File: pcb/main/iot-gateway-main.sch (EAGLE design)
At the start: 239 parts, among them CON1 6P-SH-TOP, CON2 2P-PH-TOP, CON3 2P-PH-TOP, CON4 5P-SH-TOP, CON5 3P-SH-TOP, CON6 6P-SH-TOP, Q1 AO3400, Q2 AO3400, Q3 AO3400, T1 BC817, U1 SST26VF064B, U10 BMP280, U11 CCS811, U12 ER-TFT035-6-BOT, U13 74LVC1G17, U14 LT8636, U15 MIC23159, U16 74LVC1G04, U17 LTC4040, U18 FS312F-G, U19 LTC2942, U2 EFM32GG11B820F2048GQ100, U20 FS8205, U21 LTC4313-1, U3 SST26VF016B, U4 ESP8266EX, U5 RFM69HW, U6 74LVC1G08, U7 SIM800C, U8 SI7021, U9 SI7210, X1 8 MHz, X2 32.768 kHz, X3 26 MHz

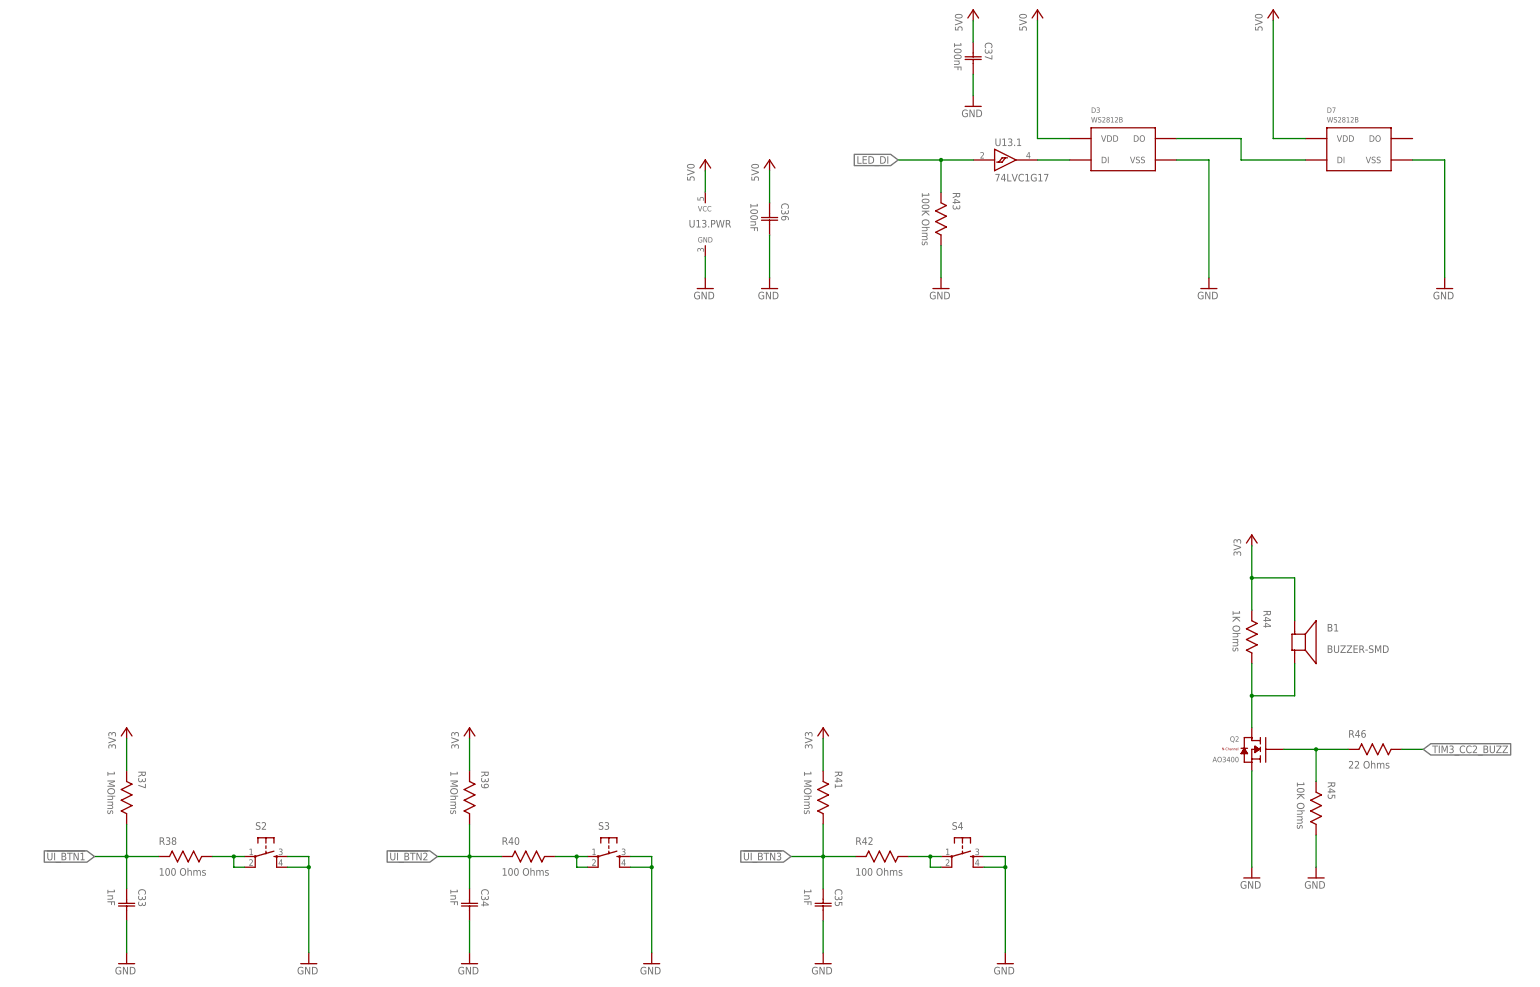
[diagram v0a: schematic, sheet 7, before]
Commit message: Place everything important inside the board space and start routing
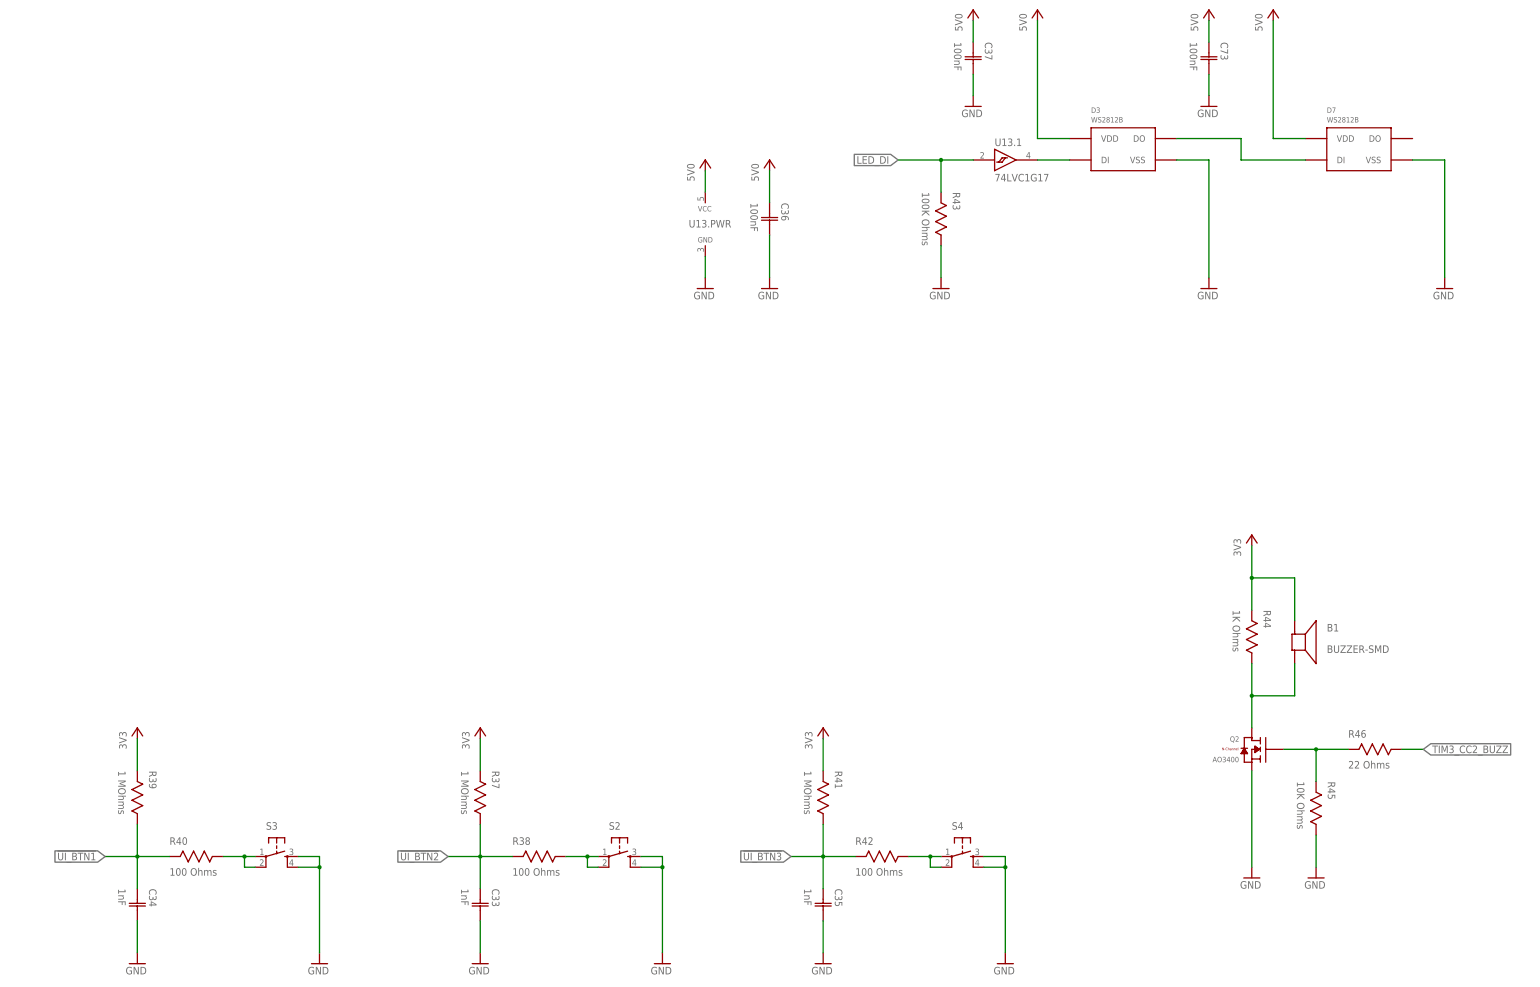
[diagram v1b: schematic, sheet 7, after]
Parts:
- added C72: 10uF, Capacitor:CAPACITOR-0603
- added C73: 100nF, Capacitor:CAPACITOR-0603
- added C74: 22uF, Capacitor:CAPACITOR-1206
- added D8: SP0502BAJT, TVS:SP0502BAJT
- C29: value 100uF -> 10uF; device Capacitor:CAPACITOR-1206 -> Capacitor:CAPACITOR-0603
- C40: VOLTAGE (none) -> 35V
- C42, C43: VOLTAGE (none) -> 50V
- C56: value 10uF -> 100nF
- C63: value 100uF -> 10uF; device Capacitor:ALUMINIUM-CAPACITOR-CASE-D -> Capacitor:CAPACITOR-1206; OCLCSC C97813 -> (none); VOLTAGE 25V -> 50V
- LOGO2: value JS-5MM -> JS-10MM; device Silkscreen:JS-5MM -> Silkscreen:JS-10MM
- X1: value 8 MHz -> 24 MHz
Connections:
- net N$1 renamed CCS811_HEATER_PWM
- net N$10 renamed WIFI_ANT_EXT
- net N$11 renamed WIFI_IO16
- net N$12 renamed 5V0_NBU_NSENS_RT
- net N$13 renamed 5V0_NBU_NSENS_SS
- net N$14 renamed 5V0_NBU_NSENS_INTVCC
- net N$15 renamed 5V0_NBU_NSENS_SW
- net N$17 renamed GSM_LED
- net N$18 renamed SIM_CLK_FILT
- net N$19 renamed LED_DI_BUF
- net N$2 renamed GSM_ANT
- net N$20 renamed BT_ANT
- net N$21 renamed BT_ANT_INT
- net N$22 renamed BT_ANT_EXT
- net N$23 renamed GSM_VRTC
- net N$25 renamed GSM_USB_D-
- net N$26 renamed GSM_USB_D+
- net N$27 renamed !GSM_PWRKEY
- net N$3 renamed SIM_RST_FILT
- net N$30 renamed GSM_USB_VBUS
- net N$31 renamed GSM_2V8
- net N$32 renamed GSM_SPK-
- net N$33 renamed TFT_BACKLIGHT_DRIVER
- net N$35 renamed BUZZ_DRV
- net N$36 renamed 5V0_NBU_NSENS_BST
- net N$38 renamed VBAT_SW
- net N$39 renamed SIM_DATA_FILT
- net N$4 renamed GSM_NETLIGHT
- net N$40 renamed BAT_CHRG_PROG
- net N$41 renamed BAT_PROT_VCC
- net N$42 renamed BAT_PROT_CS
- net N$43 renamed BAT_OC
- net N$44 renamed BAT_OD
- net N$46 renamed 3V3_SW
- net N$47 renamed 3V3_SS
- net N$48 renamed 4V2_SS
- net N$49 renamed 4V2_SW
- net N$5 renamed WIFI_BIAS
- net N$50 renamed MAIN_VREG_SW
- net N$51 renamed GSM_UART2_RX
- net N$52 renamed LED_DO
- net N$54 renamed TFT_BACKLIGHT_PWM
- net N$55 renamed GSM_SPK+
- net N$56 renamed GSM_MIC-
- net N$58 renamed GSM_UART2_TX
- net N$6 renamed WIFI_QSPI_CLK_FILT
- net N$60 renamed GSM_MIC+
- net N$61 renamed WIFI_XTAL_IN
- net N$62 renamed WIFI_XTAL_OUT
- net N$7 renamed WIFI_ANT
- net N$8 renamed WIFI_ANT_FILT
- net N$9 renamed MAIN_VDD_CORE
- net N$90 renamed 5V0_BACKUP
- net !UI_BTN1: now also C34.C1, R39.1, R40.2; no longer C33.C1, R37.1, R38.2
- net !UI_BTN2: now also C33.C1, R37.1, R38.2; no longer C34.C1, R39.1, R40.2
- net 3V3: now also C72.C1, C74.C1
- net 5V0: now also C73.C1
- net GBAT: no longer U19.GND
- net GND: now also C63.C2, C72.C2, C73.C2, C74.C2, D8.A, U19.GND; no longer C63.-
- net MAIN_HFXTAL_N: now also U2.PB14, X1.2; no longer X1.1
- net MAIN_HFXTAL_P: now also U2.PB13, X1.1; no longer X1.2
- net MAIN_LFXTAL_N: now also U2.PB8
- net MAIN_LFXTAL_P: now also U2.PB7
- net USB_D+: now also D8.C1, U2.PF11
- net USB_D-: now also D8.C2, U2.PF10
- net VIN: now also C63.C1; no longer C63.+
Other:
- moved on the sheet: C18, C33, C34, C40, C42, C56, C58, C60, C70, CON4-1, CON4-2, CON4-3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

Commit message: Connect IOs to MCU
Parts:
- removed R91: 100K Ohms, Resistor:RESISTOR-0603
- added C75: 100uF, Capacitor:CAPACITOR-1206
- added C76: 22uF, Capacitor:CAPACITOR-1206
- added U22: FS312F-G, Fortune:FS312F-G
- added U23: FS8205, Fortune:FS8205
- C18, C65: value 100nF -> 22uF; device Capacitor:CAPACITOR-0603 -> Capacitor:CAPACITOR-1206
- C20, C46, C67: value 100uF -> 100nF; device Capacitor:CAPACITOR-1206 -> Capacitor:CAPACITOR-0603
- C21: value 100nF -> 100uF; device Capacitor:CAPACITOR-0603 -> Capacitor:CAPACITOR-1206
- C22: value 33pF -> 100nF
- C23: value 1uF -> 33pF
- C24: value 33pF -> 1uF
- C25: value 100nF -> 33pF
- C29, C66, C72: value 10uF -> 100nF
- C30, C64: value 100nF -> 10uF
- C33, C35: value 1nF -> 100nF
- C37: value 100nF -> 1nF
- C39: value 4.7uF -> 1nF
- C40: value 4.7uF -> 100nF; VOLTAGE 35V -> (none)
- C41: value 470pF -> 100nF
- C42: value 1uF -> 22uF; device Capacitor:CAPACITOR-0603 -> Capacitor:CAPACITOR-1206; VOLTAGE 50V -> (none)
- C43: value 1uF -> 10uF; device Capacitor:CAPACITOR-0603 -> Capacitor:CAPACITOR-1206
- C45: value 1uF -> 22uF; device Capacitor:CAPACITOR-0603 -> Capacitor:CAPACITOR-1206
- C47: value 10nF -> 4.7uF; VOLTAGE (none) -> 35V
- C48: value 470pF -> 4.7uF
- C49: value 470pF -> 1uF; VOLTAGE (none) -> 50V
- C51: value 100nF -> 1uF; VOLTAGE (none) -> 50V
- C52: value 10pF -> 100nF
- C53: value 470pF -> 1uF
- C54: value 470pF -> 100uF; device Capacitor:CAPACITOR-0603 -> Capacitor:CAPACITOR-1206
- C55: value 100uF -> 10nF; device Capacitor:CAPACITOR-1206 -> Capacitor:CAPACITOR-0603
- C56, C58, C61, C71: value 100nF -> 470pF
- C57: value 22uF -> 470pF; device Capacitor:CAPACITOR-1206 -> Capacitor:CAPACITOR-0603
- C60: value 4.7uF -> 10pF
- C63: value 10uF -> 100uF; VOLTAGE 50V -> (none)
- C68, C70: value 22uF -> 100nF; device Capacitor:CAPACITOR-1206 -> Capacitor:CAPACITOR-0603
- C69: value 22uF -> 4.7uF; device Capacitor:CAPACITOR-1206 -> Capacitor:CAPACITOR-0603
- C74: value 22uF -> 10uF; device Capacitor:CAPACITOR-1206 -> Capacitor:CAPACITOR-0603
- CON3: value 2P-PH-TOP -> 6P-SH-TOP; device JST:2P-PH-TOP -> JST:6P-SH-TOP
- CON4: value 5P-SH-TOP -> 3P-SH-TOP; device JST:5P-SH-TOP -> JST:3P-SH-TOP
- CON5: value 3P-SH-TOP -> 5P-SH-TOP; device JST:3P-SH-TOP -> JST:5P-SH-TOP
- CON6: value 6P-SH-TOP -> 2P-PH-TOP; device JST:6P-SH-TOP -> JST:2P-PH-TOP
- D4: value LED1206-REV -> WS2812B; device LED:LED1206-REV -> LED:WS2812B-SMD5050; COLOR GREEN -> (none); PURPOSE Power Indicator -> (none)
- D5: value RED -> SMAJ24A; device LED:LED1206-REV -> TVS:SMAJ24A; COLOR RED -> (none); PURPOSE Backup Indicator -> (none)
- D6: value SMAJ24A -> SP0502BAJT; device TVS:SMAJ24A -> TVS:SP0502BAJT
- D7: value WS2812B -> LED1206-REV; device LED:WS2812B-SMD5050 -> LED:LED1206-REV; COLOR (none) -> GREEN; PURPOSE (none) -> Power Indicator
- D8: value SP0502BAJT -> RED; device TVS:SP0502BAJT -> LED:LED1206-REV; COLOR (none) -> RED; PURPOSE (none) -> Backup Indicator
- R47: value 147K Ohms -> 100K Ohms
- R48: value 21K Ohms -> 100K Ohms
- R50, R51: value 100K Ohms -> 33 Ohms
- R52: value 357K Ohms -> 100K Ohms
- R53: value 61.9K Ohms -> 4.7K Ohms
- R54: value 17.8K Ohms -> 4.7K Ohms
- R56: value 100K Ohms -> 147K Ohms
- R57: value 100K Ohms -> 21K Ohms
- R61: value 100K Ohms -> 357K Ohms
- R62: value 1M Ohms -> 61.9K Ohms
- R63: value 232K Ohms -> 17.8K Ohms
- R64: value 309K Ohms -> 100K Ohms
- R65: value 71.5K Ohms -> 100K Ohms
- R66: value 510 Ohms -> 100K Ohms
- R67: value 178K Ohms -> 100K Ohms
- R68: value 60.4K Ohms -> 100K Ohms
- R70: value 330 Ohms -> 1M Ohms
- R71: value 100K Ohms -> 232K Ohms
- R72: value 100K Ohms -> 309K Ohms
- R73: value 100K Ohms -> 71.5K Ohms
- R74: value 2K Ohms -> 510 Ohms
- R75: value 100K Ohms -> 178K Ohms
- R76: value 10m Ohms -> 60.4K Ohms; device Resistor:RESISTOR-1206 -> Resistor:RESISTOR-0603; OCLCSC C175759 -> (none)
- R77: value 100 Ohms -> 330 Ohms
- R78: value 100 Ohms -> 100K Ohms
- R80: value 1.5M Ohms -> 100K Ohms
- R81: value 274K Ohms -> 100K Ohms
- R82: value 25m Ohms -> 100K Ohms; device Resistor:RESISTOR-1206 -> Resistor:RESISTOR-0603; OCLCSC C127700 -> (none)
- R83: value 100K Ohms -> 2K Ohms
- R84: value 4.7K Ohms -> 100K Ohms
- R85: value 4.7K Ohms -> 25m Ohms; device Resistor:RESISTOR-0603 -> Resistor:RESISTOR-1206; OCLCSC (none) -> C127700
- R86: value 100K Ohms -> 10m Ohms; device Resistor:RESISTOR-0603 -> Resistor:RESISTOR-1206; OCLCSC (none) -> C175759
- R87, R88: value 100K Ohms -> 100 Ohms
- R89: value 33 Ohms -> 1.5M Ohms
- R90: value 33 Ohms -> 274K Ohms
- U13: value 74LVC1G17 -> 74LVC1G08; device Logic:74LVC1G17 -> Logic:74LVC1G08
- U14: value LT8636 -> 74LVC1G08; device Analog Devices:LT8636 -> Logic:74LVC1G08
- U15: value MIC23159 -> 74LVC1G17; device Microchip:MIC23159 -> Logic:74LVC1G17
- U16: value 74LVC1G04 -> LTC4313-1; device Logic:74LVC1G04 -> Analog Devices:LTC4313-1
- U17: value LTC4040 -> LT8636; device Analog Devices:LTC4040 -> Analog Devices:LT8636
- U18: value FS312F-G -> MIC23159; device Fortune:FS312F-G -> Microchip:MIC23159
- U19: value LTC2942 -> 74LVC1G04; device Analog Devices:LTC2942 -> Logic:74LVC1G04
- U20: value FS8205 -> LTC2942; device Fortune:FS8205 -> Analog Devices:LTC2942
- U21: value LTC4313-1 -> LTC4040; device Analog Devices:LTC4313-1 -> Analog Devices:LTC4040
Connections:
- removed net 3V3_PGOOD: R59.1, U15.PG@1
- removed net I2C0_SCL_SENS: R2.1, U10.SCK, U11.SCL, U8.SCL, U9.SCL
- removed net I2C0_SDA_SENS: R1.1, U10.SDI, U11.SDA, U8.SDA, U9.SDA
- removed net I2C1_SCL_SYS: R5.1, U12.X+/SCL, U19.SCL, U21.SCLIN
- removed net I2C1_SDA_SYS: R3.1, U12.Y+/SDA, U19.SDA, U21.SDAIN
- removed net LED_DI: R43.2, U13.1.A
- removed net US0_CS_WIFI: R15.2, U4.MTDO/IO15
- removed net US3_CS_RFM: R18.1, U5.!CS
- removed net WTIM2_CC1_TFT_BL: R30.1
- new net !UI_BTN_IRQ: U14.1.Y, U2.PB1
- new net !US0_CS_WIFI: R15.2, U2.PC8, U4.MTDO/IO15
- new net !US3_CS_RFM: R18.1, U2.PA3, U5.!CS
- new net I2C0_SCL_SYS: R5.1, U12.X+/SCL, U16.SCLIN, U2.PE5, U20.SCL
- new net I2C0_SDA_SYS: R3.1, U12.Y+/SDA, U16.SDAIN, U2.PE4, U20.SDA
- new net I2C1_SCL_SENS: R2.1, U10.SCK, U11.SCL, U2.PC5, U8.SCL, U9.SCL
- new net I2C1_SDA_SENS: R1.1, U10.SDI, U11.SDA, U2.PC4, U8.SDA, U9.SDA
- new net N$1: U13.1.Y, U14.1.A
- new net TIM4_CC2_LED_DI: R43.2, U15.1.A, U2.PF12
- new net WTIM2_CC2_TFT_BL: R30.1, U2.PA11
- net !5V0_BACKUP: now also R78.1, U19.1.A, U2.PC7, U21.!PFO; no longer R71.1, U16.1.A, U17.!PFO
- net !BAT_CHRG: now also R82.1, U2.PD7, U21.!CHRG; no longer R75.1, U17.!CHRG
- net !BAT_CHRG_EN: now also R84.1, U2.PD8, U21.CHGOFF; no longer R88.1, U17.CHGOFF
- net !BAT_FAULT: now also R81.1, U2.PD6, U21.!FAULT; no longer R73.1, U17.!FAULT
- net !CCS811_IRQ: now also U2.PE13
- net !CCS811_RESET: now also U2.PE14
- net !CCS811_WAKE: now also U2.PE12
- net !FUEL_GAUGE_IRQ: now also U2.PE10, U20.!AL!/CC; no longer U19.!AL!/CC
- net !GSM_DTR: now also U2.PC2
- net !GSM_RING: now also U2.PC1
- net !TFT_RESET: now also U2.PA14
- net !TFT_TOUCH_IRQ: now also U2.PA12
- net !TFT_TOUCH_RESET: now also U2.PA13
- net !UI_BTN1: now also R37.1, R38.2, U13.1.A, U2.PB2; no longer R39.1, R40.2
- net !UI_BTN2: now also C37.C1, R39.1, R40.2, U13.1.B, U2.PB3; no longer C33.C1, R37.1, R38.2
- net !UI_BTN3: now also C39.C1, U14.1.B, U2.PB4; no longer C35.C1
- net !US2_CS_TFT: now also U2.PA10
- net !USB_PD_IRQ: now also CON3-2.S, R49.1, U2.PE1; no longer CON6-2.S, R83.1
- net !USB_VBUS_HV_EN: now also CON5-3.S, U2.PF9; no longer CON4-3.S
- net !WIFI_RESET: now also U2.PF5
- net 3V3: now also C19.C1, C22.C1, C33.C1, C35.C1, C36.C1, C42.C1, C44.C1, C64.C1, C66.C1, C70.C1, CON3-1.S, R48.2, R49.2, R52.2, R53.2, R54.2, R65.2, R78.2, R80.2, R81.2, R82.2, U13.PWR.VCC, U14.PWR.VCC, U16.VCC, U18.SNS@1, U19.PWR.VCC; no longer C21.C1, C25.C1, C56.C1, C61.C1, C69.C1, C71.C1, C72.C1, C74.C1, CON6-1.S, R56.2, R59.2, R69.2, R71.2, R73.2, R75.2, R83.2, R85.2, R86.2, R88.2, R91.2, U15.SNS@1, U16.PWR.VCC, U21.VCC
- net 3V3_FB: now also R72.1, R73.2, U18.FB@1; no longer R64.1, R65.2, U15.FB@1
- net 3V3_SS: now also C61.C1, U18.SS@1; no longer C53.C1, U15.SS@1
- net 3V3_SW: now also U18.SW@1; no longer U15.SW@1
- net 4V2: now also C21.C1, C52.C1, C54.C1, R59.2, R61.2, U18.SNS@0; no longer C19.C1, C44.C1, C46.C1, R50.2, R52.2, U15.SNS@0
- net 4V2_EN: now also R58.2, U18.EN@0, U2.PB0; no longer R49.2, U15.EN@0
- net 4V2_FB: now also R61.1, R62.2, U18.FB@0; no longer R52.1, R53.2, U15.FB@0
- net 4V2_PGOOD: now also R65.1, U18.PG@0, U2.PE11; no longer R56.1, U15.PG@0
- net 4V2_SS: now also C57.C1, U18.SS@0; no longer C49.C1, U15.SS@0
- net 4V2_SW: now also U18.SW@0; no longer U15.SW@0
- net 4V2_VSENSE: now also C56.C1, R59.1, R60.2, U2.PD2; no longer C48.C1, R50.1, R51.2
- net 5V0: now also C40.C1, C41.C1, C45.C1, C46.C1, C48.C1, C69.C1, C75.C1, C76.C1, CON5-1.S, D4.VDD, R66.2, R89.2, U15.PWR.VCC, U18.AVIN@0, U18.AVIN@1, U18.EN@1, U18.VIN@0, U18.VIN@1, U21.F0, U21.F1, U21.F2, U21.VSYS; no longer C36.C1, C37.C1, C39.C1, C58.C1, C60.C1, C67.C1, C70.C1, C73.C1, CON4-1.S, D7.VDD, R57.2, R80.2, U13.PWR.VCC, U15.AVIN@0, U15.AVIN@1, U15.EN@1, U15.VIN@0, U15.VIN@1, U17.F0, U17.F1, U17.F2, U17.VSYS
- net 5V0_BACKUP: now also R77.2, U19.1.Y; no longer R70.2, U16.1.Y
- net 5V0_FB: now also R89.1, R90.2, U21.BSTFB, U21.RSTFB; no longer R80.1, R81.2, U17.BSTFB, U17.RSTFB
- net 5V0_ISENSE: now also C71.C1, U2.PD5, U21.CLPROG; no longer C62.C1, U17.CLPROG
- net 5V0_NBU: now also R86.1, U21.CLN; no longer R76.1, U17.CLN
- net 5V0_NBU_NSENS: now also C60.C1, C63.C1, C65.C1, C67.C1, R70.2, R74.2, R75.2, R86.2, U17.BIAS, U21.OVSNS, U21.VIN; no longer C52.C1, C55.C1, C57.C1, C59.C1, R62.2, R66.2, R67.2, R76.2, U14.BIAS, U17.OVSNS, U17.VIN
- net 5V0_NBU_NSENS_BST: now also C59.C2, U17.BST; no longer C51.C2, U14.BST
- net 5V0_NBU_NSENS_FB: now also C60.C2, R70.1, R71.2, U17.FB; no longer C52.C2, R62.1, R63.2, U14.FB
- net 5V0_NBU_NSENS_INTVCC: now also C53.C1, U17.INTVCC, U17.SYNC/MODE; no longer C45.C1, U14.INTVCC, U14.SYNC/MODE
- net 5V0_NBU_NSENS_PGOOD: now also R64.1, U17.PG, U2.PD0; no longer R55.1, U14.PG
- net 5V0_NBU_NSENS_RT: now also R63.2, U17.RT; no longer R54.2, U14.RT
- net 5V0_NBU_NSENS_SS: now also C55.C1, U17.TR/SS; no longer C47.C1, U14.TR/SS
- net 5V0_NBU_NSENS_SW: now also C59.C1, U17.SW; no longer C51.C1, U14.SW
- net 5V0_PGOOD: now also R80.1, U2.PA6, U21.!RST; no longer R72.1, U17.!RST
- net 5V0_VSENSE: now also C58.C1, R66.1, R67.2, U2.PD3; no longer C50.C1, R57.1, R58.2
- net BAT_CHRG_PROG: now also R83.2, U21.PROG; no longer R74.2, U17.PROG
- net BAT_OC: now also U22.OC, U23.G1; no longer U18.OC, U20.G1
- net BAT_OD: now also U22.OD, U23.G2; no longer U18.OD, U20.G2
- net BAT_PROT_CS: now also R88.2, U22.CS; no longer R78.2, U18.CS
- net BAT_PROT_VCC: now also R87.1, U22.VCC; no longer R77.1, U18.VCC
- net DCJACK_DET: now also CON3-5.S, R48.1, U2.PE8; no longer CON6-5.S, R69.1
- net GBAT: now also C72.C2, CON6-2.S, U22.GND, U23.S2; no longer C64.C2, CON2-2.S, U18.GND, U20.S2
- net GND: now also C51.C2, C52.C2, C64.C2, C75.C2, C76.C2, CON2-2.S, CON3-6.S, CON4-3.S, CON5-5.S, D4.VSS, D5.A, D7.C, D8.C, R47.1, R57.1, R60.1, R62.1, R67.1, R69.1, R71.1, R73.1, R76.1, R83.1, R88.1, R90.1, U14.PWR.GND, U15.PWR.GND, U16.GND, U18.AGND@0, U18.AGND@1, U18.PGND@0, U18.PGND@1, U18.PGND@2, U19.PWR.GND, U20.GND, U21.BSTOFF, U21.NTC, U23.S1; no longer C59.C2, C60.C2, C72.C2, CON3-2.S, CON4-5.S, CON5-3.S, CON6-6.S, D4.C, D5.C, D7.VSS, D8.A, R48.1, R49.1, R51.1, R53.1, R54.1, R61.1, R65.1, R68.1, R74.1, R78.1, R81.1, R87.1, U14.GND, U15.AGND@0, U15.AGND@1, U15.PGND@0, U15.PGND@1, U15.PGND@2, U16.PWR.GND, U17.BSTOFF, U17.NTC, U19.GND, U20.S1
- net GSM_LED_EN: now also U2.PB5
- net GSM_PWRKEY: now also U2.PB6
- net GSM_RF_SYNC: now also U2.PC0
- net GSM_STATUS: now also U2.PC3
- net I2C_SCL_USB_PD: now also CON3-3.S, R54.1, U16.SCLOUT; no longer CON6-3.S, R85.1, U21.SCLOUT
- net I2C_SDA_USB_PD: now also CON3-4.S, R53.1, U16.SDAOUT; no longer CON6-4.S, R84.1, U21.SDAOUT
- net LED_DI_BUF: now also U15.1.Y; no longer U13.1.Y
- net LED_DO: now also D4.DI; no longer D7.DI
- net MAG_ALERT: now also U2.PE15
- net N$37: now also U21.IGATE; no longer U17.IGATE
- net N$63: now also CON4-2.S, R51.2; no longer CON5-2.S, R90.2
- net N$64: now also CON4-1.S, R50.2; no longer CON5-1.S, R89.2
- net N$91: now also D7.A, R74.1; no longer D4.A, R66.1
- net N$92: now also D8.A, R77.1; no longer D5.A, R70.1
- net PF_THRESH: now also R75.1, R76.2, U21.PFI; no longer R67.1, R68.2, U17.PFI
- net RFM_IRQ: now also U2.PA5
- net RFM_RESET: now also U2.PA4
- net SIM_DATA: now also C25.C1; no longer C24.C1
- net SIM_VDD: now also C24.C1; no longer C22.C1
- net TIM3_CC2_BUZZ: now also U2.PA15
- net U0_CTS_GSM: now also U2.PB11
- net U0_RTS_GSM: now also U2.PB12
- net U0_RX_GSM: now also U2.PB10
- net U0_TX_GSM: now also U2.PB9
- net US0_CLK_WIFI: now also U2.PC9
- net US0_MISO_WIFI: now also U2.PC10
- net US0_MOSI_WIFI: now also U2.PC11
- net US2_CLK_TFT: now also U2.PA9
- net US2_MISO_TFT: now also U2.PA8
- net US2_MOSI_TFT: now also U2.PA7
- net US3_CLK_RFM: now also U2.PA2
- net US3_MISO_RFM: now also U2.PA1
- net US3_MOSI_RFM: now also U2.PA0
- net USB_D+: now also D6.C1, R50.1; no longer D8.C1, R89.1
- net USB_D-: now also D6.C2, R51.1; no longer D8.C2, R90.1
- net USB_PD_I2C_EN: now also R47.2, U16.ENABLE, U2.PE2; no longer R87.2, U21.ENABLE
- net USB_PD_I2C_READY: now also R52.1, U16.READY, U2.PE3; no longer R86.1, U21.READY
- net USB_VBUS_HV_STAT: now also CON5-2.S, R55.1, U2.PF8; no longer CON4-2.S, R91.1
- net USB_VBUS_SUP_EN: now also CON5-4.S, U2.PE9; no longer CON4-4.S
- net VBAT: now also C72.C1, C73.C1, C74.C1, R68.2, R85.2, R87.2, U20.VDD/SENSE+, U21.BAT; no longer C64.C1, C65.C1, C66.C1, R60.2, R77.2, R82.2, U17.BAT, U19.VDD/SENSE+
- net VBAT_NSENS: now also CON6-1.S, R85.1, U20.VBAT/SENSE-; no longer CON2-1.S, R82.1, U19.VBAT/SENSE-
- net VBAT_SW: now also U21.SW; no longer U17.SW
- net VBAT_VSENSE: now also C62.C1, R68.1, R69.2, U2.PD4; no longer C54.C1, R60.1, R61.2
- net VIN: now also C47.C1, C49.C1, C51.C1, D5.C, R56.2, U17.EN/UV, U17.VIN; no longer C40.C1, C42.C1, C63.C1, D6.C, R47.2, U14.EN/UV, U14.VIN
- net VIN_UNFUSED: now also CON2-1.S; no longer CON3-1.S
- net VIN_VSENSE: now also C50.C1, R56.1, R57.2, U2.PD1; no longer C41.C1, R47.1, R48.2
- net WIFI_EN: now also U2.PE6
- net WIFI_IRQ: now also U2.PE7

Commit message: Update libraries Finish routing Generate schematic PDF files
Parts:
- removed SJ1: (no value), Solder Jumper:SJS
- added C77: 10uF, Capacitor:CAPACITOR-0603
- added C78: 100uF, Capacitor:CAPACITOR-1206
- added C79: 22uF, Capacitor:CAPACITOR-1206
- added CON7: 2P-PH-TOP, JST:2P-PH-TOP
- added R91: 100K Ohms, Resistor:RESISTOR-0603
- added R92: 25m Ohms, Resistor:RESISTOR-1206
- added R93: 10m Ohms, Resistor:RESISTOR-1206
- added R94, R95: 100 Ohms, Resistor:RESISTOR-0603
- added R96: 1.5M Ohms, Resistor:RESISTOR-0603
- added R97: 274K Ohms, Resistor:RESISTOR-0603
- added U24: LTC4040, Analog Devices:LTC4040
- added U25: FS312F-G, Fortune:FS312F-G
- added U26: FS8205, Fortune:FS8205
- C21, C75: value 100uF -> 100nF; device Capacitor:CAPACITOR-1206 -> Capacitor:CAPACITOR-0603
- C22, C66: value 100nF -> 100uF; device Capacitor:CAPACITOR-0603 -> Capacitor:CAPACITOR-1206
- C23: value 33pF -> 100nF
- C24: value 1uF -> 33pF
- C25: value 33pF -> 1uF
- C26: value 100nF -> 33pF
- C30: value 10uF -> 100nF
- C31: value 100nF -> 1uF
- C33, C67: value 100nF -> 10uF
- C34, C39: value 1nF -> 100nF
- C38, C41: value 100nF -> 1nF
- C42, C76: value 22uF -> 100nF; device Capacitor:CAPACITOR-1206 -> Capacitor:CAPACITOR-0603
- C43: value 10uF -> 100nF; device Capacitor:CAPACITOR-1206 -> Capacitor:CAPACITOR-0603; VOLTAGE 50V -> (none)
- C46: value 100nF -> 10uF; device Capacitor:CAPACITOR-0603 -> Capacitor:CAPACITOR-1206; VOLTAGE (none) -> 50V
- C47: value 4.7uF -> 100nF; VOLTAGE 35V -> (none)
- C48: value 4.7uF -> 22uF; device Capacitor:CAPACITOR-0603 -> Capacitor:CAPACITOR-1206
- C49: value 1uF -> 100nF; VOLTAGE 50V -> (none)
- C50: value 470pF -> 4.7uF; VOLTAGE (none) -> 35V
- C51: value 1uF -> 4.7uF; VOLTAGE 50V -> (none)
- C52: value 100nF -> 1uF; VOLTAGE (none) -> 50V
- C53: value 1uF -> 470pF
- C54: value 100uF -> 1uF; device Capacitor:CAPACITOR-1206 -> Capacitor:CAPACITOR-0603; VOLTAGE (none) -> 50V
- C55: value 10nF -> 100nF
- C56: value 470pF -> 1uF
- C57: value 470pF -> 100uF; device Capacitor:CAPACITOR-0603 -> Capacitor:CAPACITOR-1206
- C58: value 470pF -> 10nF
- C59: value 100nF -> 470pF
- C60: value 10pF -> 470pF
- C62, C71: value 470pF -> 100nF
- C63: value 100uF -> 10pF; device Capacitor:CAPACITOR-1206 -> Capacitor:CAPACITOR-0603
- C64, C74: value 10uF -> 470pF
- C65: value 22uF -> 470pF; device Capacitor:CAPACITOR-1206 -> Capacitor:CAPACITOR-0603
- C68: value 100nF -> 22uF; device Capacitor:CAPACITOR-0603 -> Capacitor:CAPACITOR-1206
- C69: value 4.7uF -> 100nF
- C72: value 100nF -> 4.7uF
- CON2: value 2P-PH-TOP -> 3P-SH-TOP; device JST:2P-PH-TOP -> JST:3P-SH-TOP
- CON3: value 6P-SH-TOP -> 2P-PH-TOP; device JST:6P-SH-TOP -> JST:2P-PH-TOP
- CON4: value 3P-SH-TOP -> 6P-SH-TOP; device JST:3P-SH-TOP -> JST:6P-SH-TOP
- CON5: value 5P-SH-TOP -> 3P-SH-TOP; device JST:5P-SH-TOP -> JST:3P-SH-TOP
- CON6: value 2P-PH-TOP -> 5P-SH-TOP; device JST:2P-PH-TOP -> JST:5P-SH-TOP
- R1, R2, R3, R5: value 4.7K Ohms -> 2.2K Ohms
- R17: value 10K Ohms -> 0 Ohms
- R18, R34, R35: value 100K Ohms -> 10K Ohms
- R20, R77: value 330 Ohms -> 100K Ohms
- R21: value 10K Ohms -> 100K Ohms
- R22, R23: value 0 Ohms -> 100K Ohms
- R24, R25: value 22 Ohms -> 100K Ohms
- R26, R30: value 22 Ohms -> 0 Ohms
- R27: value 10K Ohms -> 330 Ohms
- R29: value 100K Ohms -> 0 Ohms
- R31: value 10K Ohms -> 22 Ohms
- R32: value 0 Ohms -> 22 Ohms
- R33: value 100K Ohms -> 22 Ohms
- R37, R41: value 1 MOhms -> 100K Ohms
- R38: value 100 Ohms -> 22 Ohms
- R39: value 1 MOhms -> 10K Ohms
- R40: value 100 Ohms -> 0 Ohms
- R42, R87, R88: value 100 Ohms -> 100K Ohms
- R44: value 1K Ohms -> 100K Ohms; MF VISHAY -> (none)
- R45: value 10K Ohms -> 1 MOhms; MF VISHAY -> (none)
- R46: value 22 Ohms -> 100 Ohms; MF VISHAY -> (none)
- R47: value 100K Ohms -> 1 MOhms
- R48: value 100K Ohms -> 100 Ohms
- R50: value 33 Ohms -> 1 MOhms
- R51: value 33 Ohms -> 100 Ohms
- R52: value 100K Ohms -> 1K Ohms; MF (none) -> VISHAY
- R53: value 4.7K Ohms -> 10K Ohms; MF (none) -> VISHAY
- R54: value 4.7K Ohms -> 22 Ohms; MF (none) -> VISHAY
- R56: value 147K Ohms -> 100K Ohms
- R57: value 21K Ohms -> 100K Ohms
- R58, R59: value 100K Ohms -> 33 Ohms
- R61: value 357K Ohms -> 4.7K Ohms
- R62: value 61.9K Ohms -> 4.7K Ohms
- R63: value 17.8K Ohms -> 100K Ohms
- R64: value 100K Ohms -> 147K Ohms
- R65: value 100K Ohms -> 21K Ohms
- R69: value 100K Ohms -> 357K Ohms
- R70: value 1M Ohms -> 61.9K Ohms
- R71: value 232K Ohms -> 17.8K Ohms
- R72: value 309K Ohms -> 100K Ohms
- R73: value 71.5K Ohms -> 100K Ohms
- R74: value 510 Ohms -> 100K Ohms
- R75: value 178K Ohms -> 100K Ohms
- R76: value 60.4K Ohms -> 100K Ohms
- R78: value 100K Ohms -> 1M Ohms
- R79: value 100K Ohms -> 232K Ohms
- R80: value 100K Ohms -> 309K Ohms
- R81: value 100K Ohms -> 71.5K Ohms
- R82: value 100K Ohms -> 510 Ohms
- R83: value 2K Ohms -> 178K Ohms
- R84: value 100K Ohms -> 57.6K Ohms
- R85: value 25m Ohms -> 330 Ohms; device Resistor:RESISTOR-1206 -> Resistor:RESISTOR-0603; OCLCSC C127700 -> (none)
- R86: value 10m Ohms -> 100K Ohms; device Resistor:RESISTOR-1206 -> Resistor:RESISTOR-0603; OCLCSC C175759 -> (none)
- R89: value 1.5M Ohms -> 100K Ohms
- R90: value 274K Ohms -> 2K Ohms
- U10: value BMP280 -> SIM800C; device Bosch:BMP280 -> SimCom:SIM800C
- U11: value CCS811 -> SI7021; device AMS:CCS811 -> Silicon Labs:SI7021
- U12: value ER-TFT035-6-BOT -> SI7210; device BuyDisplay:ER-TFT035-6-BOT -> Silicon Labs:SI7210
- U13: value 74LVC1G08 -> BMP280; device Logic:74LVC1G08 -> Bosch:BMP280
- U14: value 74LVC1G08 -> CCS811; device Logic:74LVC1G08 -> AMS:CCS811
- U15: value 74LVC1G17 -> TMG39933; device Logic:74LVC1G17 -> AMS:TMG39933
- U16: value LTC4313-1 -> ER-TFT035-6-BOT; device Analog Devices:LTC4313-1 -> BuyDisplay:ER-TFT035-6-BOT
- U17: value LT8636 -> 74LVC1G11; device Analog Devices:LT8636 -> Logic:74LVC1G11
- U18: value MIC23159 -> 74LVC1G17; device Microchip:MIC23159 -> Logic:74LVC1G17
- U19: value 74LVC1G04 -> LTC4313-1; device Logic:74LVC1G04 -> Analog Devices:LTC4313-1
- U20: value LTC2942 -> LT8636; device Analog Devices:LTC2942 -> Analog Devices:LT8636
- U21: value LTC4040 -> MIC23159; device Analog Devices:LTC4040 -> Microchip:MIC23159
- U22: value FS312F-G -> 74LVC1G04; device Fortune:FS312F-G -> Logic:74LVC1G04
- U23: value FS8205 -> LTC2942; device Fortune:FS8205 -> Analog Devices:LTC2942
- U6: value 74LVC1G08 -> 74LVC1G332; device Logic:74LVC1G08 -> Logic:74LVC1G332
- U7: value SIM800C -> 74LVC1G332; device SimCom:SIM800C -> Logic:74LVC1G332
- U8: value SI7021 -> 74LVC1G32; device Silicon Labs:SI7021 -> Logic:74LVC1G32
- U9: value SI7210 -> 74LVC1G08; device Silicon Labs:SI7210 -> Logic:74LVC1G08
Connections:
- net LED_DO renamed LED2_DI
- net US3_CLK_RFM renamed US3_CLK_ISM
- net US3_MISO_RFM renamed US3_MISO_ISM
- net US3_MOSI_RFM renamed US3_MOSI_ISM
- removed net !CCS811_IRQ: R29.1, U11.!INT, U2.PE13
- removed net !CCS811_RESET: R27.1, U11.!RESET, U2.PE14
- removed net !CCS811_WAKE: R28.1, U11.!WAKE, U2.PE12
- removed net !GSM_RING: U2.PC1, U7.UART1_RI
- removed net !US3_CS_RFM: R18.1, U2.PA3, U5.!CS
- removed net 5V0_PGOOD: R80.1, U2.PA6, U21.!RST
- removed net LED_DI_BUF: D3.DI, U15.1.Y
- removed net MAG_ALERT: U2.PE15, U9.ALERT
- removed net N$1: U13.1.Y, U14.1.A
- removed net RFM_IRQ: R19.2, U2.PA5, U5.IO0
- removed net RFM_RESET: R17.2, U2.PA4, U5.RST
- removed net U0_CTS_GSM: U2.PB11, U7.UART1_CTS
- removed net U0_RTS_GSM: U2.PB12, U7.UART1_RTS
- removed net U0_RX_GSM: U2.PB10, U7.UART1_TXD
- removed net U0_TX_GSM: U2.PB9, U7.UART1_RXD
- removed net WIFI_IO16: SJ1.1, U4.XPD_DCDC/IO16
- removed net WTIM2_CC2_TFT_BL: R30.1, U2.PA11
- new net !ALS_IRQ: R37.1, U15.!INT, U2.PA6
- new net !IAQ_IRQ: R36.1, U14.!INT, U2.PE13
- new net !IAQ_RESET: R34.1, U14.!RESET, U2.PE14
- new net !IAQ_WAKE: R35.1, U14.!WAKE, U2.PE12
- new net !US3_CS_ISM: R19.1, U2.PA3, U5.!CS
- new net EXT_LED_DI: CON2-2.S, D4.DO
- new net ISM_IRQ: R26.1, U2.PA5, U8.1.Y
- new net ISM_IRQ0: R20.2, R26.2, U5.IO0, U6.1.A
- new net ISM_IRQ012: U6.1.Y, U8.1.A
- new net ISM_IRQ1: R21.2, U5.IO1, U6.1.B
- new net ISM_IRQ2: R22.2, U5.IO2, U6.1.C
- new net ISM_IRQ3: R23.2, U5.IO3, U7.1.A
- new net ISM_IRQ345: U7.1.Y, U8.1.B
- new net ISM_IRQ4: R24.2, U5.IO4, U7.1.B
- new net ISM_IRQ5: R25.2, U5.IO5, U7.1.C
- new net ISM_RESET: R18.2, U2.PA4, U5.RST
- new net LED1_DI: D3.DI, U18.1.Y
- new net MAG_IRQ: U12.ALERT, U2.PE15
- new net N$2: U15.LDR, U15.LEDK
- new net TIM0_CC1_TFT_BL: R38.1, U2.PC0
- new net U1_CTS_GSM: U10.UART1_CTS, U2.PB11
- new net U1_RTS_GSM: U10.UART1_RTS, U2.PB12
- new net U1_RX_GSM: U10.UART1_TXD, U2.PB10
- new net U1_TX_GSM: U10.UART1_RXD, U2.PB9
- new net WIFI_RTC_WKUP: R17.1, U4.XPD_DCDC/IO16
- net !5V0_BACKUP: now also R87.1, U22.1.A, U24.!PFO; no longer R78.1, U19.1.A, U21.!PFO
- net !BAT_CHRG: now also R89.1, U24.!CHRG; no longer R82.1, U21.!CHRG
- net !BAT_CHRG_EN: now also R91.1, U24.CHGOFF; no longer R84.1, U21.CHGOFF
- net !BAT_FAULT: now also R88.1, U24.!FAULT; no longer R81.1, U21.!FAULT
- net !FUEL_GAUGE_IRQ: now also R86.1, U23.!AL!/CC; no longer R79.1, U20.!AL!/CC
- net !GSM_DTR: now also U10.UART1_DTR; no longer U7.UART1_DTR
- net !GSM_PWRKEY: now also U10.PWRKEY; no longer U7.PWRKEY
- net !TFT_RESET: now also R41.1, U16.!RESET; no longer R33.1, U12.!RESET
- net !TFT_TOUCH_IRQ: now also R44.1, U16.X-/!IRQ!; no longer R36.1, U12.X-/!IRQ!
- net !TFT_TOUCH_RESET: now also R43.1, U16.Y-/!RST!; no longer R35.1, U12.Y-/!RST!
- net !UI_BTN1: now also C37.C1, R45.1, R46.2, U17.1.C; no longer C34.C1, R37.1, R38.2, U13.1.A
- net !UI_BTN2: now also C38.C1, R47.1, R48.2, U17.1.A; no longer C37.C1, R39.1, R40.2, U13.1.B
- net !UI_BTN3: now also C41.C1, R50.1, R51.2, U17.1.B; no longer C39.C1, R41.1, R42.2, U14.1.B
- net !UI_BTN_IRQ: now also U17.1.Y; no longer U14.1.Y
- net !US2_CS_TFT: now also R42.1, U16.!CS; no longer R34.1, U12.!CS
- net !USB_PD_IRQ: now also CON4-2.S, R57.1; no longer CON3-2.S, R49.1
- net !USB_VBUS_HV_EN: now also CON6-3.S; no longer CON5-3.S
- net !WIFI_RESET: now also R17.2; no longer SJ1.2
- net 3V3: now also C20.C1, C23.C1, C34.C1, C39.C1, C45.C1, C47.C1, C67.C1, C69.C1, C73.C1, CON4-1.S, R19.2, R42.2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; no longer C22.C1, C26.C1, C42.C1, C44.C1, C64.C1, C66.C1, C70.C1, CON3-1.S, R18.2, R27.2, R28.2, R29.2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
- net 3V3_FB: now also R80.1, R81.2, U21.FB@1; no longer R72.1, R73.2, U18.FB@1
- net 3V3_SS: now also C64.C1, U21.SS@1; no longer C61.C1, U18.SS@1
- net 3V3_SW: now also U21.SW@1; no longer U18.SW@1
- net 4V2: now also C22.C1, C55.C1, C57.C1, R67.2, R69.2, U10.VBAT@0, U10.VBAT@1, U21.SNS@0; no longer C20.C1, C52.C1, C54.C1, R59.2, R61.2, U18.SNS@0, U7.VBAT@0, U7.VBAT@1
- net 4V2_EN: now also R66.2, U21.EN@0; no longer R58.2, U18.EN@0
- net 4V2_FB: now also R69.1, R70.2, U21.FB@0; no longer R61.1, R62.2, U18.FB@0
- net 4V2_PGOOD: now also R73.1, U21.PG@0; no longer R65.1, U18.PG@0
- net 4V2_SS: now also C60.C1, U21.SS@0; no longer C57.C1, U18.SS@0
- net 4V2_SW: now also U21.SW@0; no longer U18.SW@0
- net 4V2_VSENSE: now also C59.C1, R67.1, R68.2; no longer C56.C1, R59.1, R60.2
- net 5V0: now also C42.C1, C43.C1, C44.C1, C49.C1, C51.C1, C71.C1, C72.C1, C78.C1, C79.C1, CON2-1.S, CON6-1.S, R74.2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; no longer C38.C1, C41.C1, C45.C1, C46.C1, C68.C1, C69.C1, C75.C1, C76.C1, CON5-1.S, R66.2, R89.2, U15.PWR.VCC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
- net 5V0_BACKUP: now also R85.2, U22.1.Y; no longer R77.2, U19.1.Y
- net 5V0_FB: now also R96.1, R97.2, U24.BSTFB, U24.RSTFB; no longer R89.1, R90.2, U21.BSTFB, U21.RSTFB
- net 5V0_ISENSE: now also C74.C1, U24.CLPROG; no longer C71.C1, U21.CLPROG
- net 5V0_NBU: now also R93.1, U24.CLN; no longer R86.1, U21.CLN
- net 5V0_NBU_NSENS: now also C66.C1, C68.C1, C70.C1, R78.2, R82.2, R83.2, R93.2, U20.BIAS, U24.OVSNS, U24.VIN; no longer C60.C1, C65.C1, C67.C1, R70.2, R74.2, R75.2, R86.2, U17.BIAS, U21.OVSNS, U21.VIN
- net 5V0_NBU_NSENS_BST: now also C62.C2, U20.BST; no longer C59.C2, U17.BST
- net 5V0_NBU_NSENS_FB: now also C63.C2, R78.1, R79.2, U20.FB; no longer C60.C2, R70.1, R71.2, U17.FB
- net 5V0_NBU_NSENS_INTVCC: now also C56.C1, U20.INTVCC, U20.SYNC/MODE; no longer C53.C1, U17.INTVCC, U17.SYNC/MODE
- net 5V0_NBU_NSENS_PGOOD: now also R72.1, U20.PG; no longer R64.1, U17.PG
- net 5V0_NBU_NSENS_RT: now also R71.2, U20.RT; no longer R63.2, U17.RT
- net 5V0_NBU_NSENS_SS: now also C58.C1, U20.TR/SS; no longer C55.C1, U17.TR/SS
- net 5V0_NBU_NSENS_SW: now also C62.C1, U20.SW; no longer C59.C1, U17.SW
- net 5V0_VSENSE: now also C61.C1, R74.1, R75.2; no longer C58.C1, R66.1, R67.2
- net BAT_CHRG_PROG: now also R90.2, U24.PROG; no longer R83.2, U21.PROG
- net BAT_OC: now also U25.OC, U26.G1; no longer U22.OC, U23.G1
- net BAT_OD: now also U25.OD, U26.G2; no longer U22.OD, U23.G2
- net BAT_PROT_CS: now also R95.2, U25.CS; no longer R88.2, U22.CS
- net BAT_PROT_VCC: now also R94.1, U25.VCC; no longer R87.1, U22.VCC
- net BT_ANT: now also R29.1, R30.2, U10.BT_ANT; no longer R22.1, R23.2, U7.BT_ANT
- net BT_ANT_EXT: now also R30.1; no longer R23.1
- net BT_ANT_INT: now also R29.2; no longer R22.2
- net BUZZ_DRV: now also R52.1; no longer R44.1
- net CCS811_HEATER_PWM: now also U14.PWM, U14.SENSE; no longer U11.PWM, U11.SENSE
- net DCJACK_DET: now also CON4-5.S, R56.1; no longer CON3-5.S, R48.1
- net GBAT: now also C75.C2, CON7-2.S, U25.GND, U26.S2; no longer C72.C2, CON6-2.S, U22.GND, U23.S2
- net GND: now also C59.C2, C60.C2, C72.C2, C77.C2, C78.C2, C79.C2, CON2-3.S, CON3-2.S, CON4-6.S, CON5-3.S, CON6-5.S, R18.1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; no longer C62.C2, C63.C2, C75.C2, CON2-2.S, CON3-6.S, CON4-3.S, CON5-5.S, R17.1, R19.1, R31.1, R43.1, R45.1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
- net GSM_2V8: now also U10.VDD_EXT; no longer U7.VDD_EXT
- net GSM_ANT: now also U10.GSM_ANT; no longer U7.GSM_ANT
- net GSM_LED: now also U9.1.Y; no longer U6.1.Y
- net GSM_LED_EN: now also U9.1.A; no longer U6.1.A
- net GSM_MIC+: now also U10.MICP; no longer U7.MICP
- net GSM_MIC-: now also U10.MICN; no longer U7.MICN
- net GSM_NETLIGHT: now also U10.NETLIGHT, U9.1.B; no longer U6.1.B, U7.NETLIGHT
- net GSM_PWRKEY: now also R28.2; no longer R21.2
- net GSM_RF_SYNC: now also U10.RF_SYNC, U2.PC1; no longer U2.PC0, U7.RF_SYNC
- net GSM_SPK+: now also U10.SPKP; no longer U7.SPKP
- net GSM_SPK-: now also U10.SPKN; no longer U7.SPKN
- net GSM_STATUS: now also U10.STATUS; no longer U7.STATUS
- net GSM_UART2_RX: now also U10.UART2_RXD; no longer U7.UART2_RXD
- net GSM_UART2_TX: now also U10.UART2_TXD; no longer U7.UART2_TXD
- net GSM_USB_D+: now also U10.USB_DP; no longer U7.USB_DP
- net GSM_USB_D-: now also U10.USB_DM; no longer U7.USB_DM
- net GSM_USB_VBUS: now also U10.USB_VBUS; no longer U7.USB_VBUS
- net GSM_VRTC: now also U10.VRTC; no longer U7.VRTC
- net I2C0_SCL_SYS: now also U16.X+/SCL, U19.SCLIN, U23.SCL; no longer U12.X+/SCL, U16.SCLIN, U20.SCL
- net I2C0_SDA_SYS: now also U16.Y+/SDA, U19.SDAIN, U23.SDA; no longer U12.Y+/SDA, U16.SDAIN, U20.SDA
- net I2C1_SCL_SENS: now also U12.SCL, U13.SCK, U14.SCL, U15.SCL; no longer U10.SCK, U8.SCL, U9.SCL
- net I2C1_SDA_SENS: now also U12.SDA, U13.SDI, U14.SDA, U15.SDA; no longer U10.SDI, U8.SDA, U9.SDA
- net I2C_SCL_USB_PD: now also CON4-3.S, R62.1, U19.SCLOUT; no longer CON3-3.S, R54.1, U16.SCLOUT
- net I2C_SDA_USB_PD: now also CON4-4.S, R61.1, U19.SDAOUT; no longer CON3-4.S, R53.1, U16.SDAOUT
- net N$16: now also R27.2; no longer R20.2
- net N$24: now also R38.2, R39.2; no longer R30.2, R31.2
- net N$28: now also R28.1; no longer R21.1
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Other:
- note added: "!ALS_IRQ! - EXTI5"
- note added: "!FUEL_GAUGE_IRQ! - EXTI8"
- note added: "!IAQ_IRQ! - EXTI13"
- note added: "!TFT_TOUCH_IRQ! - EXTI12"
- note added: "!USB_PD_IRQ! - EXTI3"
- note added: "EXTI0 - !UI_BTN_IRQ!"
- note added: "GSM_RF_SYNC - EXTI1"
- note added: "GSM_STATUS - EXTI2"
- note added: "I2C0 - SCL - System Management - Location 7"
- note added: "I2C0 - SDA - System Management - Location 7"
- note added: "I2C1 - SCL - Sensors - Location 0"
- note added: "I2C1 - SDA - Sensors - Location 0"
- note added: "ISM_IRQ - EXTI4"
- note added: "Location 2 - GSM/Bluetooth Radio - CTS - U1"
- note added: "Location 2 - GSM/Bluetooth Radio - RTS - U1"
- note added: "Location 2 - GSM/Bluetooth Radio - RX - U1"
- note added: "Location 2 - GSM/Bluetooth Radio - TX - U1"
- note added: "MAG_IRQ - EXTI14"
- note added: "TIM0 - Channel 1 - TFT Backlight - Location 3"
- note added: "TIM3 - Channel 2 - Buzzer - Location 0"
- note added: "US0 - !CS! - Wi-Fi Radio - Location 2"
- note added: "US0 - CLK - Wi-Fi Radio - Location 2"
- note added: "US0 - MISO - Wi-Fi Radio - Location 2"
- note added: "US0 - MOSI - Wi-Fi Radio - Location 2"
- note added: "US2 - !CS! - TFT Display - Location 2"
- note added: "US2 - CLK - TFT Display - Location 2"
- note added: "US2 - MISO - TFT Display - Location 2"
- note added: "US2 - MOSI - TFT Display - Location 2"
- note added: "US3 - !CS! - ISM Radio - Location 0"
- note added: "US3 - CLK - ISM Radio - Location 0"
- note added: "US3 - MISO - ISM Radio - Location 0"
- note added: "US3 - MOSI - ISM Radio - Location 0"
- note added: "Vbkpstart = 1.19 / (R75/(R75+R76))"
- note added: "Vout = ((R78/R79) + 1) * 0.97"
- note added: "Vout = ((R96/R97) + 1) * 0.8"
- note added: "WIFI_IRQ - EXTI6"
- note removed: "Vout = ((R62/R63) + 1) * 0.97"
- note removed: "Vout = ((R80/R81) + 1) * 0.8"

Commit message: Maybe finished?
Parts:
- added TP13, TP14: TESTPOINT-1.27MM, PADs:TESTPOINT-1.27MM
- R95: value 100 Ohms -> 2K Ohms
- renumbered U26 to Q4
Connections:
- net TFT_DC renamed TFT_D/!C!
- removed net 5V0_ISENSE: C74.C1, U2.PD5, U24.CLPROG
- new net !GSM_DCD: TP14.TP, U10.UART1_DCD
- new net !GSM_RING: TP13.TP, U10.UART1_RI
- new net 5V0_NBU_ISENSE: C74.C1, U2.PD4, U24.CLPROG
- net VBAT_VSENSE: now also U2.PD5; no longer U2.PD4
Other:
- note added: "For LiPo use FS312F-G For Li-ion use DW01A-G"
- moved on the sheet: B1, C75, Q2, R52, R53, R54, R94, R95, U25
